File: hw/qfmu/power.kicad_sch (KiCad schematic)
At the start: 4 parts, among them U10 BQ7694202PFBR

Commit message: feat: add new BLDC controler and RF section
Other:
- company: Daniel Pérez -> Daniel Enrique Pérez Díaz
- title: (none) -> Quincy FMU
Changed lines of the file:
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@@
 	(paper "A4")
 	(title_block
-		(date "2024-09-10")
+		(title "Quincy FMU")
+		(date "2024-09-28")
 		(rev "0")
-		(company "Daniel Pérez")
+		(company "Daniel Enrique Pérez Díaz")
+		(comment 1 "Flight Management Unit for the Quincy Quadcopter project.")
 	)
 	(junction

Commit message: feat: finish motors, RF and power monitor
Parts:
- added C56, C57, C58, C59, C65: 0.22u, Capacitor_SMD:C_0805_2012Metric_Pad1.18x1.45mm_HandSolder, symbol Device:C
- added C60, C66: 1u, Capacitor_SMD:C_0805_2012Metric_Pad1.18x1.45mm_HandSolder, symbol Device:C
- added C61, C64: 100p, Capacitor_SMD:C_0805_2012Metric_Pad1.18x1.45mm_HandSolder, symbol Device:C
- added C62: 0.47u, Capacitor_SMD:C_0805_2012Metric_Pad1.18x1.45mm_HandSolder, symbol Device:C
- added C63, C69, C70: 0.1u, Capacitor_SMD:C_0805_2012Metric_Pad1.18x1.45mm_HandSolder, symbol Device:C
- added C67, C68: 10u, Capacitor_SMD:C_0805_2012Metric_Pad1.18x1.45mm_HandSolder, symbol Device:C
- added C71, C72: 22u, Capacitor_SMD:C_0805_2012Metric_Pad1.18x1.45mm_HandSolder, symbol Device:C
- added D5, D6: D_Schottky, Diode_SMD:D_SOD-123, symbol Device:D_Schottky
- added FUSE1: ITV5432L1230WR, QFN4_ITV5432_LTF, symbol ITV5432L5030:ITV5432L5030WR
- added L5: VLS5045EX-3R3N, VLS5045EX-3R3N:IND_VLS5045EX-3R3N, symbol VLS5045EX-3R3N:VLS5045EX-3R3N
- added Q27, Q29, Q30, Q31: IRF540N, Package_TO_SOT_THT:TO-220-3_Horizontal_TabDown, symbol Transistor_FET:IRF540N
- added Q28: FCX495TA, SOT89_DIO, symbol FCX495TA:FCX495TA
- added R20: 5m, Resistor_SMD:R_2512_6332Metric_Pad1.40x3.35mm_HandSolder, symbol Device:R
- added R21, R22, R23, R24: 20, Resistor_SMD:R_0805_2012Metric_Pad1.20x1.40mm_HandSolder, symbol Device:R
- added R25, R26, R27: 100, Resistor_SMD:R_0805_2012Metric_Pad1.20x1.40mm_HandSolder, symbol Device:R
- added R28, R29, R36, R37: 10k, Resistor_SMD:R_0805_2012Metric_Pad1.20x1.40mm_HandSolder, symbol Device:R
- added R30, R31, R32, R33: 10M, Resistor_SMD:R_0805_2012Metric_Pad1.20x1.40mm_HandSolder, symbol Device:R
- added R34, R35: 3.9k, Resistor_SMD:R_0805_2012Metric_Pad1.20x1.40mm_HandSolder, symbol Device:R
- added R38: 30.9k, Resistor_SMD:R_0805_2012Metric_Pad1.20x1.40mm_HandSolder, symbol Device:R
- added R39, R40: 4.7k, Resistor_SMD:R_0805_2012Metric_Pad1.20x1.40mm_HandSolder, symbol Device:R
- added TH1, TH2, TH3: Thermistor_NTC, Resistor_SMD:R_0603_1608Metric_Pad0.98x0.95mm_HandSolder, symbol Device:Thermistor_NTC
- added U14: TPS562202, Package_TO_SOT_SMD:SOT-563, symbol Regulator_Switching:TPS562202
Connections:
- net +12V: now also C67.2, C68.2, C69.2, Q27.3 (S), R28.2, R29.2, R31.1, R34.2, R36.1, U14.1 (VIN); no longer CELL1.1 (+)
- net PACK_NEG: now also R20.1, R21.1, R26.1
- net VCELL1: now also R22.1
- net VCELL2: now also R23.1
- net at U10.13 (VC3): now also C59.2, R24.2
- net at U10.14 (VC2): now also C58.2, C59.1, R23.2
- net at U10.15 (VC1): now also C57.2, C58.1, R22.2
- net at U10.16 (VC0): now also C56.2, R21.2
- net GND: now reaches U10.17 (VSS)
- net GND: now also C56.1, C57.1, C60.1, C61.1, C65.1, C66.1, C67.1, C68.1, C69.1, C71.1, C72.1, R20.2, R27.1, R38.1, TH1.2, TH2.2, TH3.2, U14.3 (GND)
- net at U10.18 (SRP): now also C63.2, C64.2, R26.2
- net at U10.20 (SRN): now also C63.1, C64.1, R27.2
- net at U10.21 (TS1): now also TH1.1
- net at U10.22 (TS2): now also TH2.1
- net at U10.23 (TS3): now also TH3.1
- net at U10.24 (REG18): now also C65.2
- net MON_ALERT: now reaches U10.25 (ALERT)
- net MON_SCL: now reaches U10.26 (SCL)
- net MON_SCL: now also R39.2
- net MON_SDA: now reaches U10.27 (SDA)
- net MON_SDA: now also R40.2
- net DCHG: now reaches U10.31 (DCHG)
- net DDSG: now reaches U10.32 (DDSG)
- net MON_RST_SHUT: now reaches U10.33 (RST_SHUT)
- net at U10.36 (REGIN): now also Q28.3 (E)
- net at U10.37 (BREG): now also Q28.1 (B)
- net FUSE: now reaches U10.38 (FUSE)
- net FUSE: now also FUSE1.2
- net PDSG: now reaches U10.39 (PDSG)
- net PDSG: now also Q30.1 (G), R33.2
- net PCHG: now reaches U10.40 (PCHG)
- net PCHG: now also Q31.1 (G), R32.1
- net at U10.41 (LD): now also R28.1
- net at U10.42 (PACK): now also R29.1
- net at U10.43 (DSG): now also Q27.1 (G), R31.2
- net at U10.45 (CHG): now also Q29.1 (G), R30.1
- net at U10.46 (CP1): now also C62.2
- net at U10.47 (BAT): now also C60.2, C61.2, C62.1, R25.2
- new net: C70.1, L5.2, U14.2 (SW)
- new net: C70.2, U14.4 (VBST)
- new net: Q31.3 (S), R35.2
- new net: FUSE1.1, Q29.3 (S), R30.2, R35.1
- new net: C66.2, D6.1 (K), Q28.2 (C)
- new net: R37.1, R38.2, U14.6 (VFB)
- new net: Q30.3 (S), R34.1
- new net: D5.1 (K), R25.1
- new net: R36.2, U14.5 (EN)
- new net +3.3V: C71.2, C72.2, L5.1, R37.2, R39.1, R40.1
- new net CMN_DRAIN: D6.2 (A), Q27.2 (D), Q29.2 (D), Q30.2 (D), Q31.2 (D), R32.2, R33.1
- new net VCELL3: CELL1.1 (+), D5.2 (A), FUSE1.3, R24.1
- no-connect marks 0 -> 20
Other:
- moved on the sheet: CELL1, CELL2, CELL3, U10

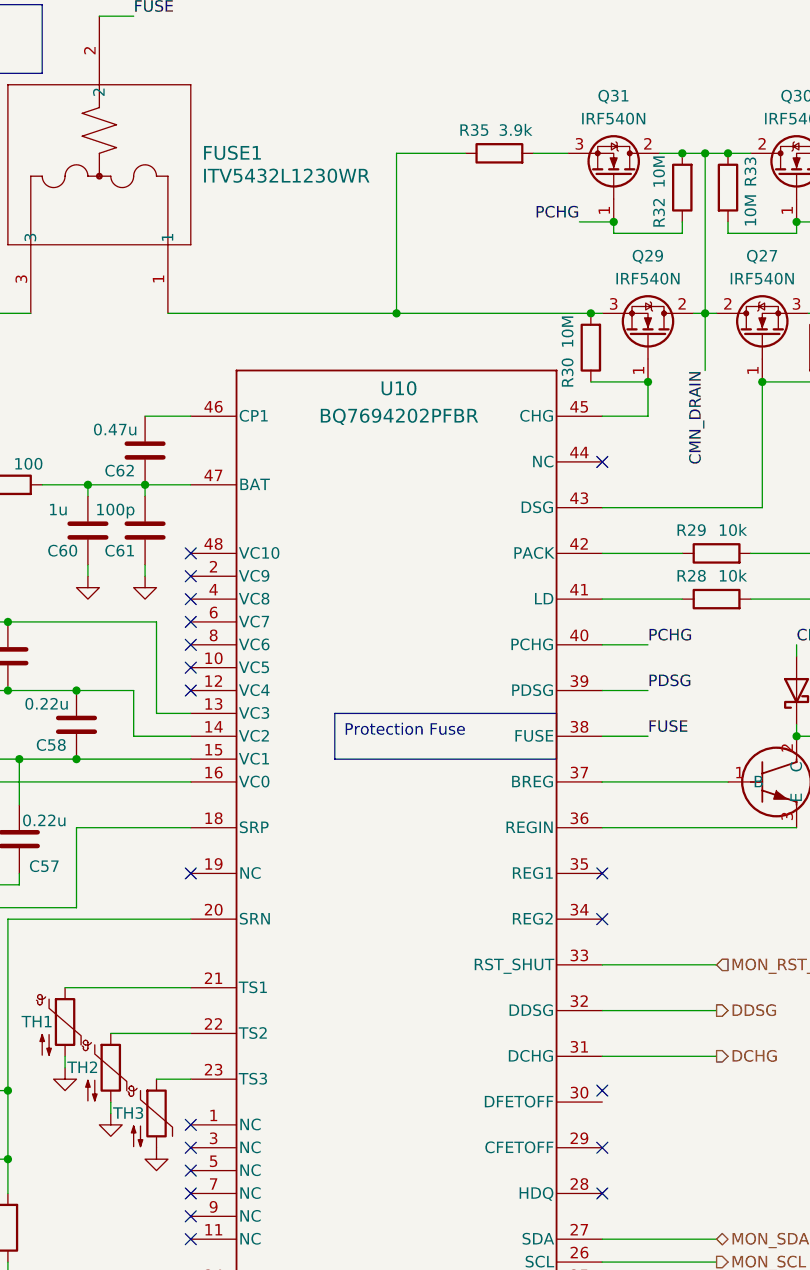
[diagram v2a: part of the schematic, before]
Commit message: feat: start PCB design, define board outline and basic placement
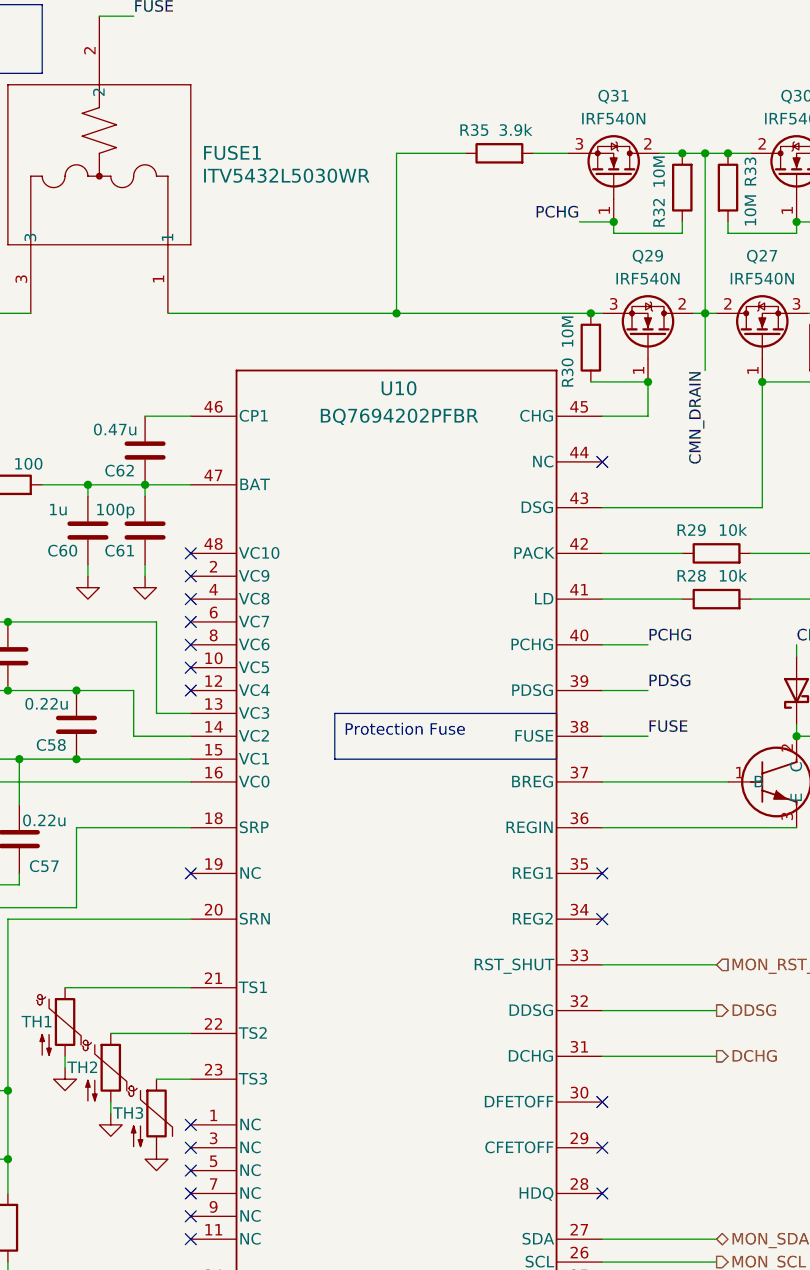
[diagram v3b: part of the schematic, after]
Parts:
- FUSE1: value ITV5432L1230WR -> ITV5432L5030WR
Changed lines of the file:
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@@
 	)
 	(no_connect
-		(at 161.29 137.16)
+		(at 161.29 138.43)
 	)
 	(no_connect
@@
 	)
 	(symbol
+		(lib_id "ITV5432L5030:ITV5432L5030WR")
+		(at 97.79 50.8 90)
+		(unit 1)
+		(exclude_from_sim no)
+		(in_bom yes)
+		(on_board yes)
+		(dnp no)
+		(fields_autoplaced yes)
+		(property "Reference" "FUSE1"
+			(at 116.84 33.0199 90)
+			(effects
+				(font
+					(size 1.524 1.524)
+				)
+				(justify right)
+			)
+		)
+		(property "Value" "ITV5432L5030WR"
+			(at 116.84 35.5599 90)
+			(effects
+				(font
+					(size 1.524 1.524)
+				)
+				(justify right)
+			)
+		)
+		(property "Footprint" "QFN4_ITV5432_LTF"
+			(at 97.79 50.8 0)
+			(effects
+				(font
+					(size 1.27 1.27)
+					(italic yes)
+				)
+				(hide yes)
+			)
+		)
+		(property "Datasheet" "ITV5432L5030WR"
+			(at 97.79 50.8 0)
+			(effects
+				(font
+					(size 1.27 1.27)
+					(italic yes)
+				)
+				(hide yes)
+			)
+		)
+		(property "Description" ""
+			(at 97.79 50.8 0)
+			(effects
+				(font
+					(size 1.27 1.27)
+				)
+				(hide yes)
+			)
+		)
+		(pin "1"
+		)
+		(pin "2"
+		)
+		(pin "3"
+		)
+		(instances
+			(project ""
+				(path "/ce683e6e-7873-406a-bf15-47714980a4b3/4c8652b6-b347-476a-a7b2-7473c68247e5"
+					(reference "FUSE1")
+					(unit 1)
+				)
+			)
+		)
+	)
+	(symbol
 		(lib_id "power:GND")
 		(at 236.22 39.37 0)
@@
 					(unit 1)
 				)
-			)
-		)
-	)
-	(symbol
-		(lib_id "ITV5432L5030:ITV5432L5030WR")
-		(at 97.79 50.8 90)
-		(unit 1)
-		(exclude_from_sim no)
-		(in_bom yes)
-		(on_board yes)
-		(dnp no)
-		(fields_autoplaced yes)
-		(property "Reference" "FUSE1"
-			(at 116.84 33.0199 90)
-			(effects
-				(font
-					(size 1.524 1.524)
-				)
-				(justify right)
-			)
-		)
-		(property "Value" "ITV5432L1230WR"
-			(at 116.84 35.5599 90)
-			(effects
-				(font
-					(size 1.524 1.524)
-				)
-				(justify right)
-			)
-		)
-		(property "Footprint" "QFN4_ITV5432_LTF"
-			(at 97.79 50.8 0)
-			(effects
-				(font
-					(size 1.27 1.27)
-					(italic yes)
-				)
-				(hide yes)
-			)
-		)
-		(property "Datasheet" "ITV5432L5030WR"
-			(at 97.79 50.8 0)
-			(effects
-				(font
-					(size 1.27 1.27)
-					(italic yes)
-				)
-				(hide yes)
-			)
-		)
-		(property "Description" ""
-			(at 97.79 50.8 0)
-			(effects
-				(font
-					(size 1.27 1.27)
-				)
-				(hide yes)
-			)
-		)
-		(pin "3"
-		)
-		(pin "2"
-		)
-		(pin "1"
-		)
-		(instances
-			(project ""
-				(path "/ce683e6e-7873-406a-bf15-47714980a4b3/4c8652b6-b347-476a-a7b2-7473c68247e5"
-					(reference "FUSE1")
-					(unit 1)
-				)

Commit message: feat: reposition elements and go back to original edgecuts
Position elements for easier routing and start from scratch.
Revert shape design to be fully symmetrical.
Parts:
- added PWRIN1: TestPoint, Connector_Pin:Pin_D0.7mm_L6.5mm_W1.8mm_FlatFork, symbol Connector:TestPoint
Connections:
- net +12V: now also PWRIN1.1
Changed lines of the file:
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@@
 	)
 	(junction
+		(at 210.82 36.83)
+		(diameter 0)
+		(color 0 0 0 0)
+	)
+	(junction
 		(at 219.71 50.8)
 		(diameter 0)
@@
 	(wire
 		(pts
+			(xy 210.82 36.83) (xy 210.82 40.64)
+		)
+		(stroke
+			(width 0)
+			(type default)
+		)
+	)
+	(wire
+		(pts
 			(xy 87.63 114.3) (xy 96.52 114.3)
 		)
@@
 	(wire
 		(pts
+			(xy 210.82 36.83) (xy 215.9 36.83)
+		)
+		(stroke
+			(width 0)
+			(type default)
+		)
+	)
+	(wire
+		(pts
 			(xy 95.25 166.37) (xy 101.6 166.37)
 		)
@@
 	(symbol
 		(lib_id "power:+12V")
-		(at 210.82 40.64 0)
+		(at 210.82 36.83 0)
 		(unit 1)
 		(exclude_from_sim no)
@@
 		(dnp no)
 		(property "Reference" "#PWR024"
-			(at 210.82 44.45 0)
+			(at 210.82 40.64 0)
 			(effects
 				(font
@@
 		)
 		(property "Value" "+12V"
-			(at 210.82 36.322 0)
+			(at 210.82 33.02 0)
 			(effects
 				(font
@@
 		)
 		(property "Footprint" ""
-			(at 210.82 40.64 0)
+			(at 210.82 36.83 0)
 			(effects
 				(font
@@
 		)
 		(property "Datasheet" ""
-			(at 210.82 40.64 0)
+			(at 210.82 36.83 0)
 			(effects
 				(font
@@
 		)
 		(property "Description" "Power symbol creates a global label with name \"+12V\""
-			(at 210.82 40.64 0)
+			(at 210.82 36.83 0)
 			(effects
 				(font
@@
 					(unit 1)
 				)
+			)
+		)
+	)
+	(symbol
+		(lib_id "Connector:TestPoint")
+		(at 215.9 36.83 270)
+		(unit 1)
+		(exclude_from_sim no)
+		(in_bom yes)
+		(on_board yes)
+		(dnp no)
+		(property "Reference" "PWRIN1"
+			(at 214.63 35.306 90)
+			(effects
+				(font
+					(size 1.27 1.27)
+				)
+				(justify left)
+			)
+		)
+		(property "Value" "TestPoint"
+			(at 217.9321 39.37 0)
+			(effects
+				(font
+					(size 1.27 1.27)
+				)
+				(justify left)
+				(hide yes)
+			)
+		)
+		(property "Footprint" "Connector_Pin:Pin_D0.7mm_L6.5mm_W1.8mm_FlatFork"
+			(at 215.9 41.91 0)
+			(effects
+				(font
+					(size 1.27 1.27)
+				)
+				(hide yes)
+			)
+		)
+		(property "Datasheet" "~"
+			(at 215.9 41.91 0)
+			(effects
+				(font
+					(size 1.27 1.27)
+				)
+				(hide yes)
+			)
+		)
+		(property "Description" "test point"
+			(at 215.9 36.83 0)
+			(effects
+				(font
+					(size 1.27 1.27)
+				)
+				(hide yes)
+			)
+		)
+		(pin "1"
+		)
+		(instances
+			(project "qfmu"
+				(path "/ce683e6e-7873-406a-bf15-47714980a4b3/4c8652b6-b347-476a-a7b2-7473c68247e5"
+					(reference "PWRIN1")
+					(unit 1)
+				)
